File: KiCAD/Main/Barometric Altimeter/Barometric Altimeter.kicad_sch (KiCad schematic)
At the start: 3 parts

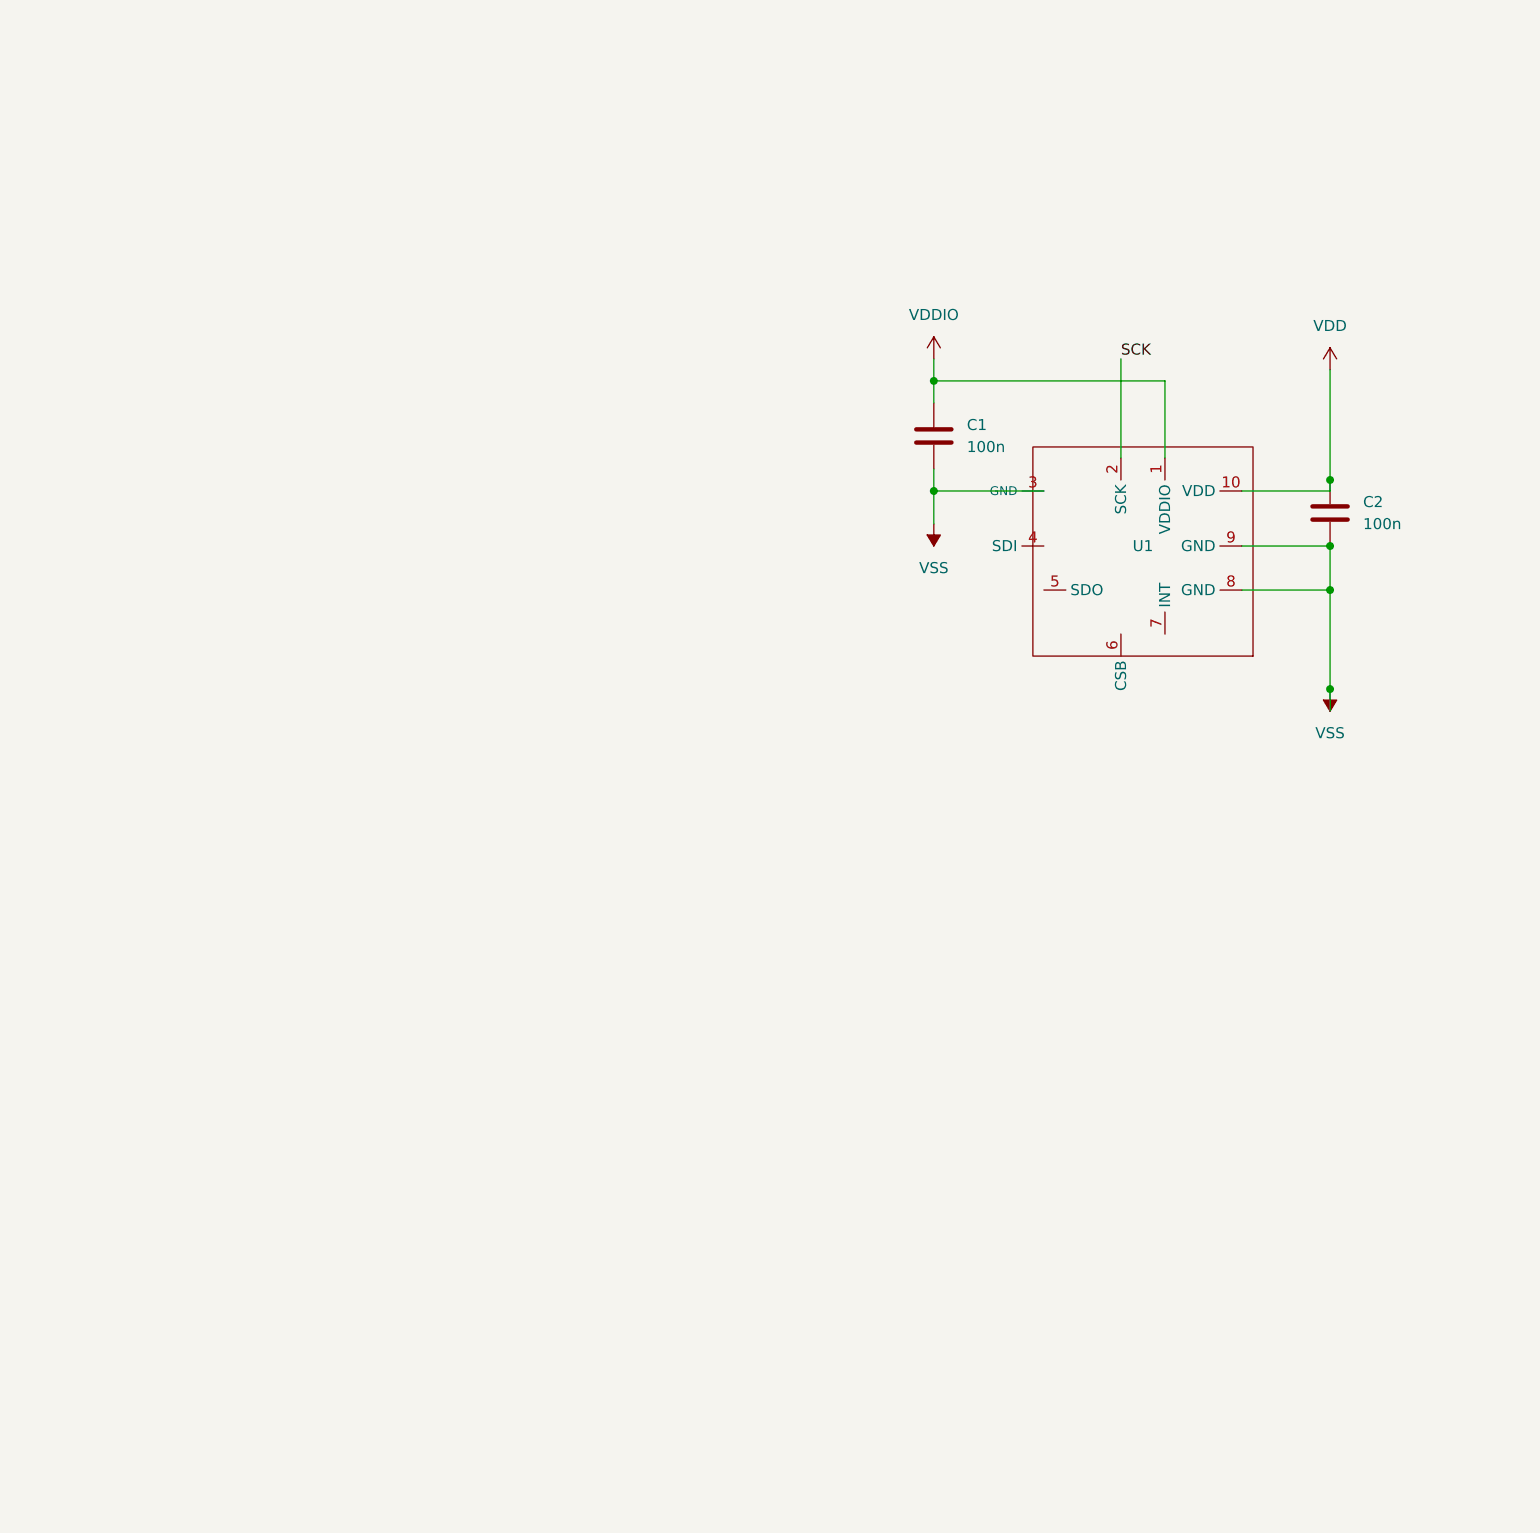
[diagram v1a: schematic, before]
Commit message: Remove thermocouples due to complexity and focus switch
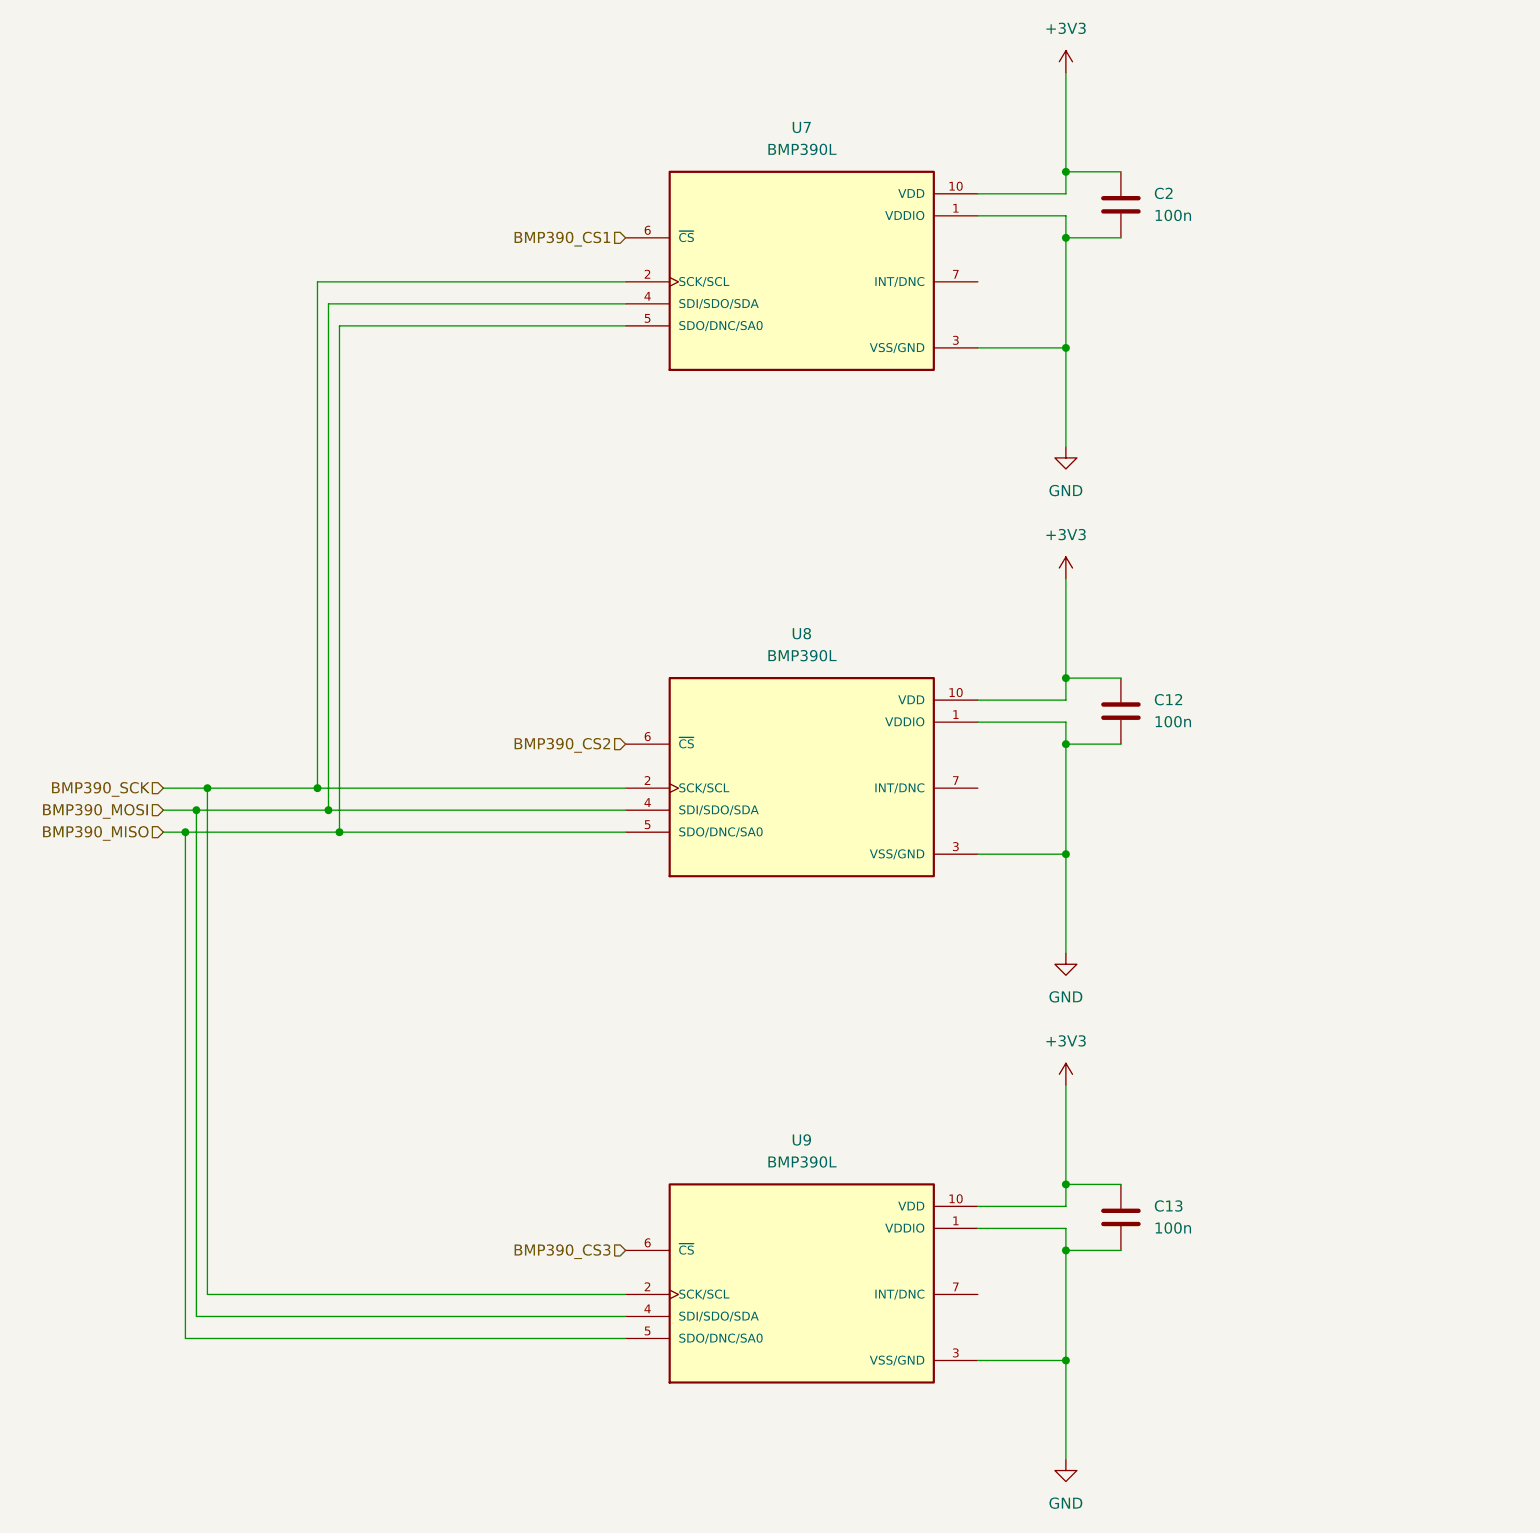
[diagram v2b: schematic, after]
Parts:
- removed C1: 100n, symbol Device:C
- removed U1: ~, symbol BMP390_project:BMP390
- added C12, C13: 100n, symbol Device:C
- added U7, U8, U9: BMP390L, BMP390L:XDCR_BMP390L, symbol BMP390L:BMP390L
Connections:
- net VDD renamed +3V3
- net +3V3: now also C12.1, C13.1, U7.10 (VDD), U8.10 (VDD), U9.10 (VDD)
- net VSS renamed GND
- net GND: now also C12.2, C13.2, U7.1 (VDDIO), U7.3 (VSS/GND), U7.8 (VSS/GND), U7.9 (VSS/GND), U8.1 (VDDIO), U8.3 (VSS/GND), U8.8 (VSS/GND), U8.9 (VSS/GND), U9.1 (VDDIO), U9.3 (VSS/GND), U9.8 (VSS/GND), U9.9 (VSS/GND)
- new net BMP390_CS1: U7.6 (~{CS})
- new net BMP390_CS2: U8.6 (~{CS})
- new net BMP390_CS3: U9.6 (~{CS})
- new net BMP390_MISO: U7.5 (SDO/DNC/SA0), U8.5 (SDO/DNC/SA0), U9.5 (SDO/DNC/SA0)
- new net BMP390_MOSI: U7.4 (SDI/SDO/SDA), U8.4 (SDI/SDO/SDA), U9.4 (SDI/SDO/SDA)
- new net BMP390_SCK: U7.2 (SCK/SCL), U8.2 (SCK/SCL), U9.2 (SCK/SCL)
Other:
- moved on the sheet: C2

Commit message: Polish for review
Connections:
- net +3V3: now also U7.1 (VDDIO), U8.1 (VDDIO), U9.1 (VDDIO)
- net GND: no longer U7.1 (VDDIO), U8.1 (VDDIO), U9.1 (VDDIO)
- net BMP390 INT2: now reaches U8.7 (INT/DNC)
- net BMP390 INT1: now reaches U7.7 (INT/DNC)
- net BMP390 INT3: now reaches U9.7 (INT/DNC)
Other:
- moved on the sheet: C12, C13, C2

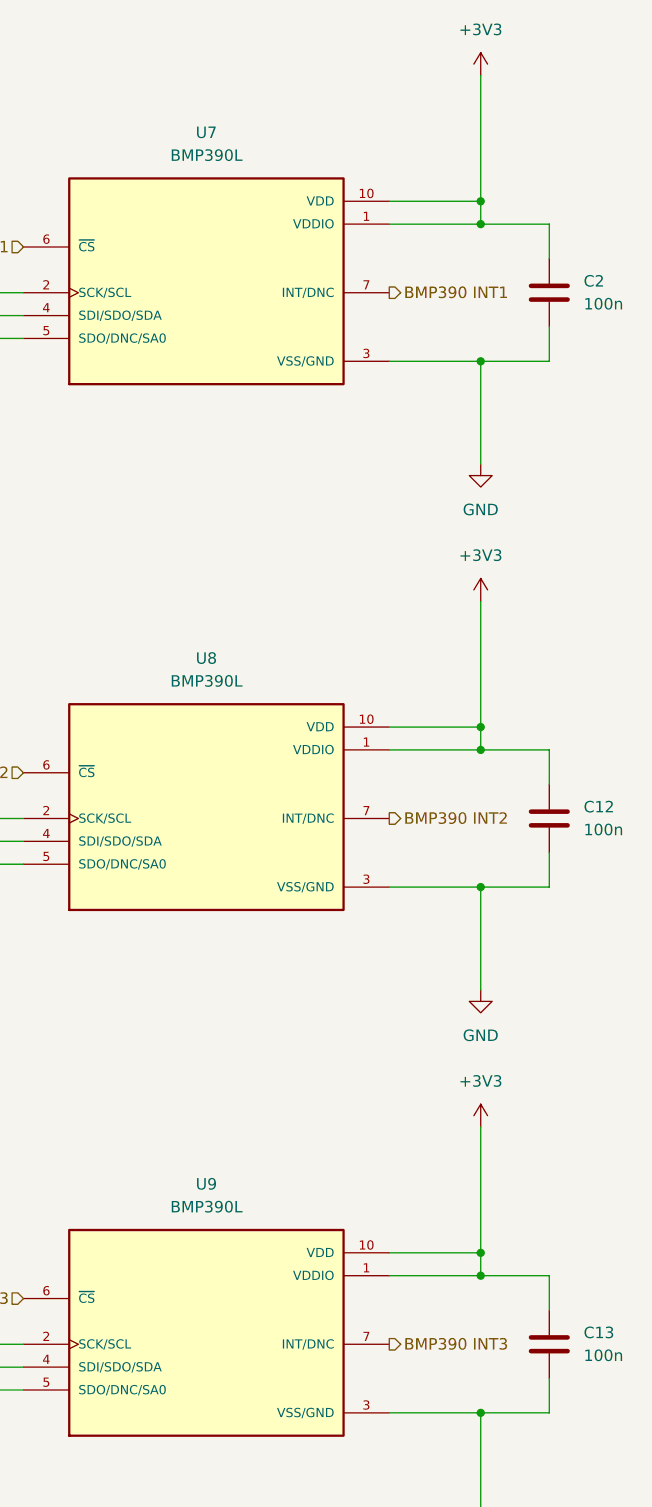
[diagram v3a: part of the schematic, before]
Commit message: Create wiring diagram draft
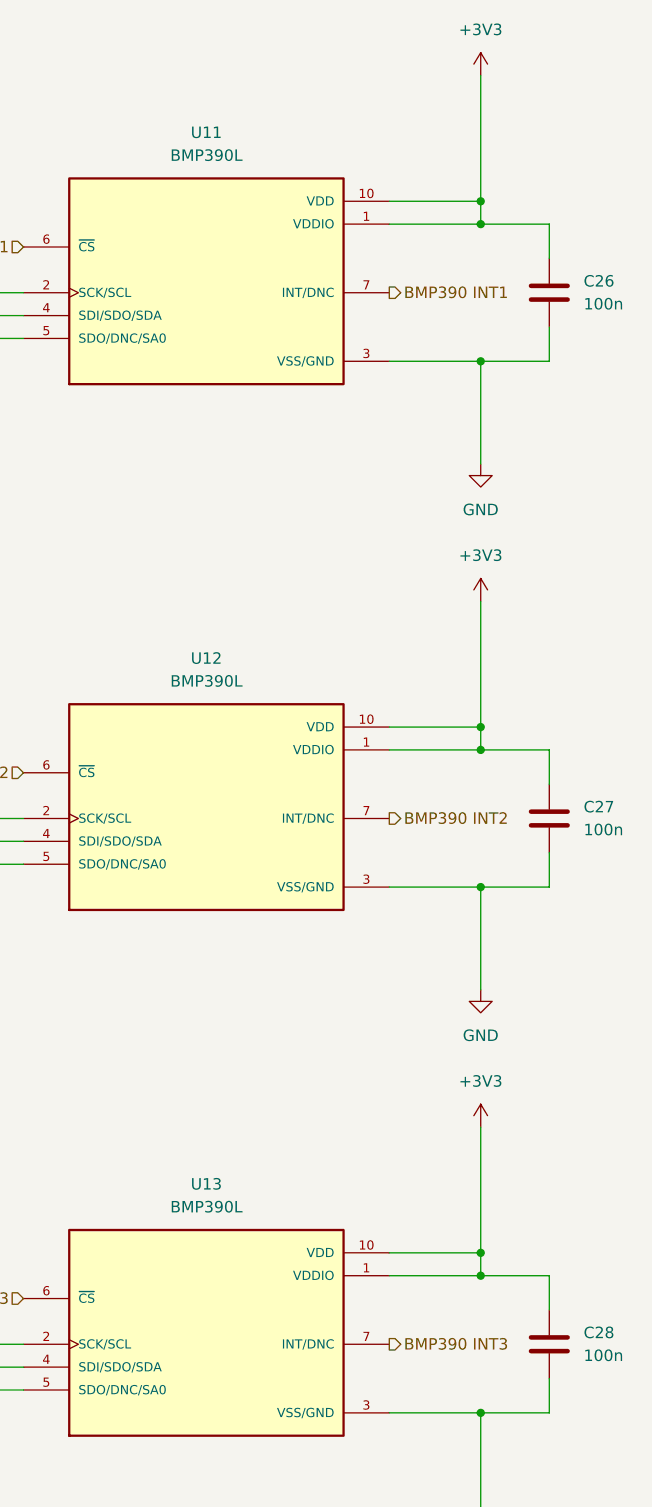
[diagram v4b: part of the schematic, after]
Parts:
- renumbered C2 to C26, C12 to C27, C13 to C28, U7 to U11, U8 to U12, U9 to U13
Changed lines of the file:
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@@
 		(dnp no)
 		(fields_autoplaced yes)
-		(property "Reference" "#PWR031"
+		(property "Reference" "#PWR058"
 			(at 134.62 191.77 0)
 			(effects
@@
 			(project "Main"
 				(path "/bbb10697-a5dd-43b8-9c6f-4c5919cf3463/8b42f0c3-8c9e-485f-8d18-4bee19125eba"
-					(reference "#PWR031")
+					(reference "#PWR058")
 					(unit 1)
 				)
@@
 		(dnp no)
 		(fields_autoplaced yes)
-		(property "Reference" "U8"
+		(property "Reference" "U12"
 			(at 104.14 90.17 0)
 			(effects
@@
 			(project "Main"
 				(path "/bbb10697-a5dd-43b8-9c6f-4c5919cf3463/8b42f0c3-8c9e-485f-8d18-4bee19125eba"
-					(reference "U8")
+					(reference "U12")
 					(unit 1)
 				)
@@
 		(dnp no)
 		(fields_autoplaced yes)
-		(property "Reference" "U7"
+		(property "Reference" "U11"
 			(at 104.14 31.75 0)
 			(effects
@@
 			(project ""
 				(path "/bbb10697-a5dd-43b8-9c6f-4c5919cf3463/8b42f0c3-8c9e-485f-8d18-4bee19125eba"
-					(reference "U7")
+					(reference "U11")
 					(unit 1)
 				)
@@
 		(dnp no)
 		(fields_autoplaced yes)
-		(property "Reference" "C12"
+		(property "Reference" "C27"
 			(at 146.05 106.6799 0)
 			(effects
@@
 			(project "Main"
 				(path "/bbb10697-a5dd-43b8-9c6f-4c5919cf3463/8b42f0c3-8c9e-485f-8d18-4bee19125eba"
-					(reference "C12")
+					(reference "C27")
 					(unit 1)
 				)
@@
 		(dnp no)
 		(fields_autoplaced yes)
-		(property "Reference" "U9"
+		(property "Reference" "U13"
 			(at 104.14 148.59 0)
 			(effects
@@
 			(project "Main"
 				(path "/bbb10697-a5dd-43b8-9c6f-4c5919cf3463/8b42f0c3-8c9e-485f-8d18-4bee19125eba"
-					(reference "U9")
+					(reference "U13")
 					(unit 1)
 				)
@@
 		(dnp no)
 		(fields_autoplaced yes)
-		(property "Reference" "#PWR029"
+		(property "Reference" "#PWR056"
 			(at 134.62 133.35 0)
 			(effects
@@
 			(project "Main"
 				(path "/bbb10697-a5dd-43b8-9c6f-4c5919cf3463/8b42f0c3-8c9e-485f-8d18-4bee19125eba"
-					(reference "#PWR029")
+					(reference "#PWR056")
 					(unit 1)
 				)
@@
 		(dnp no)
 		(fields_autoplaced yes)
-		(property "Reference" "#PWR030"
+		(property "Reference" "#PWR057"
 			(at 134.62 146.05 0)
 			(effects
@@
 			(project "Main"
 				(path "/bbb10697-a5dd-43b8-9c6f-4c5919cf3463/8b42f0c3-8c9e-485f-8d18-4bee19125eba"
-					(reference "#PWR030")
+					(reference "#PWR057")
 					(unit 1)
 				)
@@
 		(dnp no)
 		(fields_autoplaced yes)
-		(property "Reference" "#PWR028"
+		(property "Reference" "#PWR055"
 			(at 134.62 87.63 0)
 			(effects
@@
 			(project "Main"
 				(path "/bbb10697-a5dd-43b8-9c6f-4c5919cf3463/8b42f0c3-8c9e-485f-8d18-4bee19125eba"
-					(reference "#PWR028")
+					(reference "#PWR055")
 					(unit 1)
 				)
@@
 		(dnp no)
 		(fields_autoplaced yes)
-		(property "Reference" "#PWR026"
+		(property "Reference" "#PWR053"
 			(at 134.62 29.21 0)
 			(effects
@@
 			(project ""
 				(path "/bbb10697-a5dd-43b8-9c6f-4c5919cf3463/8b42f0c3-8c9e-485f-8d18-4bee19125eba"
-					(reference "#PWR026")
+					(reference "#PWR053")
 					(unit 1)
 				)
@@
 		(dnp no)
 		(fields_autoplaced yes)
-		(property "Reference" "C13"
+		(property "Reference" "C28"
 			(at 146.05 165.0999 0)
 			(effects
@@
 			(project "Main"
 				(path "/bbb10697-a5dd-43b8-9c6f-4c5919cf3463/8b42f0c3-8c9e-485f-8d18-4bee19125eba"
-					(reference "C13")
+					(reference "C28")
 					(unit 1)
 				)
@@
 		(dnp no)
 		(fields_autoplaced yes)
-		(property "Reference" "C2"
+		(property "Reference" "C26"
 			(at 146.05 48.2599 0)
 			(effects
@@
 			(project ""
 				(path "/bbb10697-a5dd-43b8-9c6f-4c5919cf3463/8b42f0c3-8c9e-485f-8d18-4bee19125eba"
-					(reference "C2")
+					(reference "C26")
 					(unit 1)
 				)
@@
 		(dnp no)
 		(fields_autoplaced yes)
-		(property "Reference" "#PWR027"
+		(property "Reference" "#PWR054"
 			(at 134.62 74.93 0)
 			(effects
@@
 			(project ""
 				(path "/bbb10697-a5dd-43b8-9c6f-4c5919cf3463/8b42f0c3-8c9e-485f-8d18-4bee19125eba"
-					(reference "#PWR027")
+					(reference "#PWR054")
 					(unit 1)
 				)
